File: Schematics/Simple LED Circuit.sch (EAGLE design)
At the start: 3 parts

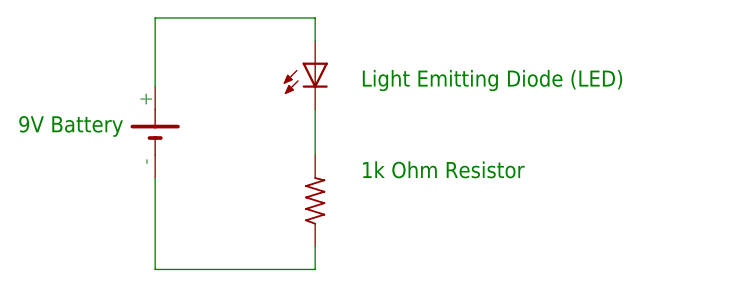
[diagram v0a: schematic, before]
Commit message: Cleaned up schematics' labeling.
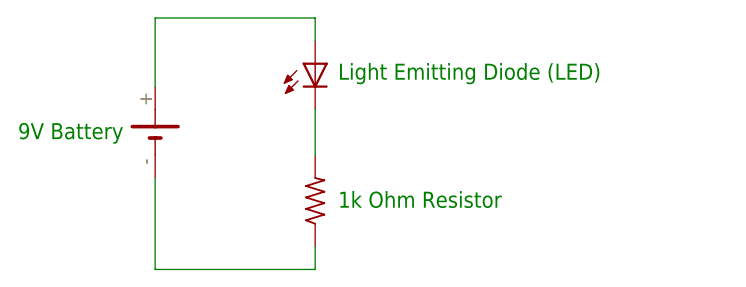
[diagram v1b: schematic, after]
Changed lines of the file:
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@@
 <?xml version="1.0" encoding="utf-8"?>
 <!DOCTYPE eagle SYSTEM "eagle.dtd">
-<eagle version="6.6.0">
+<eagle version="9.4.2">
 <drawing>
 <settings>
 <setting alwaysvectorfont="no"/>
+<setting keepoldvectorfont="yes"/>
 <setting verticaltext="up"/>
 </settings>
-<grid distance="0.1" unitdist="inch" unit="inch" style="lines" multiple="1" display="no" altdistance="0.01" altunitdist="inch" altunit="inch"/>
+<grid distance="0.1" unitdist="inch" unit="inch" style="lines" multiple="1" display="yes" altdistance="0.01" altunitdist="inch" altunit="inch"/>
 <layers>
 <layer number="1" name="Top" color="4" fill="1" visible="no" active="no"/>
@@
 <sheet>
 <plain>
-<text x="40.64" y="58.42" size="1.778" layer="91">9V Battery</text>
-<text x="78.74" y="53.34" size="1.778" layer="91">1k Ohm Resistor</text>
-<text x="78.74" y="63.5" size="1.778" layer="91">Light Emitting Diode (LED)</text>
+<text x="40.64" y="57.658" size="1.778" layer="91">9V Battery</text>
+<text x="76.2" y="50.038" size="1.778" layer="91">1k Ohm Resistor</text>
+<text x="76.2" y="64.262" size="1.778" layer="91">Light Emitting Diode (LED)</text>
 </plain>
 <instances>
